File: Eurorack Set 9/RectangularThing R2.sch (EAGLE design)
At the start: 176 parts, among them IC1 CEM3310, IC2 TL074D, IC3 CEM3320, IC4 CEM3310, IC5 TL074D, IC7 CEM3340, U1 LM4040DIM3-5.0

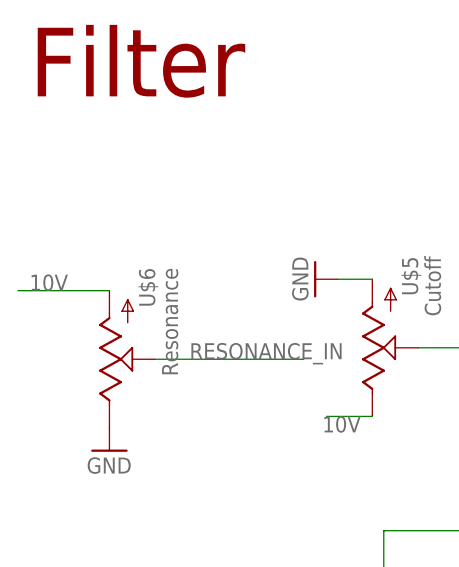
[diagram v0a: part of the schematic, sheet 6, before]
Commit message: Stabilize pitch control in RectangularTHing
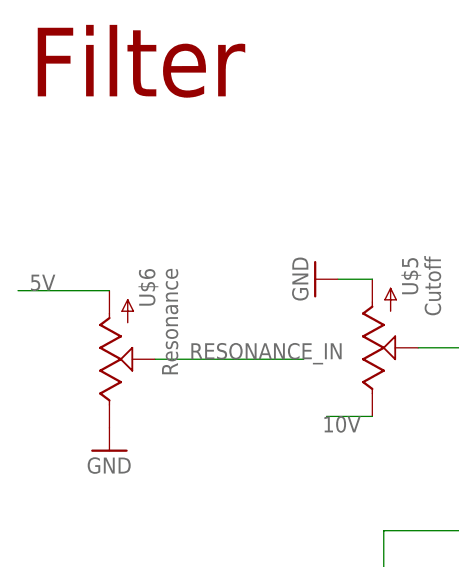
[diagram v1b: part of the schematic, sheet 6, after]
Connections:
- net 10V: no longer U$6.A
- net 5V: now also U$6.A
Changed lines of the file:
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@@
 <net name="10V" class="1">
-<segment>
-<pinref part="U$6" gate="G$1" pin="A"/>
-<wire x1="3.81" y1="102.87" x2="-6.35" y2="102.87" width="0.1524" layer="91"/>
-<label x="-5.08" y="102.87" size="1.778" layer="95"/>
-</segment>
 <segment>
 <pinref part="U$5" gate="G$1" pin="E"/>
@@
 </segment>
 </net>
+<net name="5V" class="1">
+<segment>
+<pinref part="U$6" gate="G$1" pin="A"/>
+<wire x1="3.81" y1="102.87" x2="-6.35" y2="102.87" width="0.1524" layer="91"/>
+<label x="-5.08" y="102.87" size="1.778" layer="95"/>
+</segment>
+</net>
